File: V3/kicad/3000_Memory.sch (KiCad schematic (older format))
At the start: 4 parts, among them U3000 SST39SF040, U3001 AS6C4008-55PCN

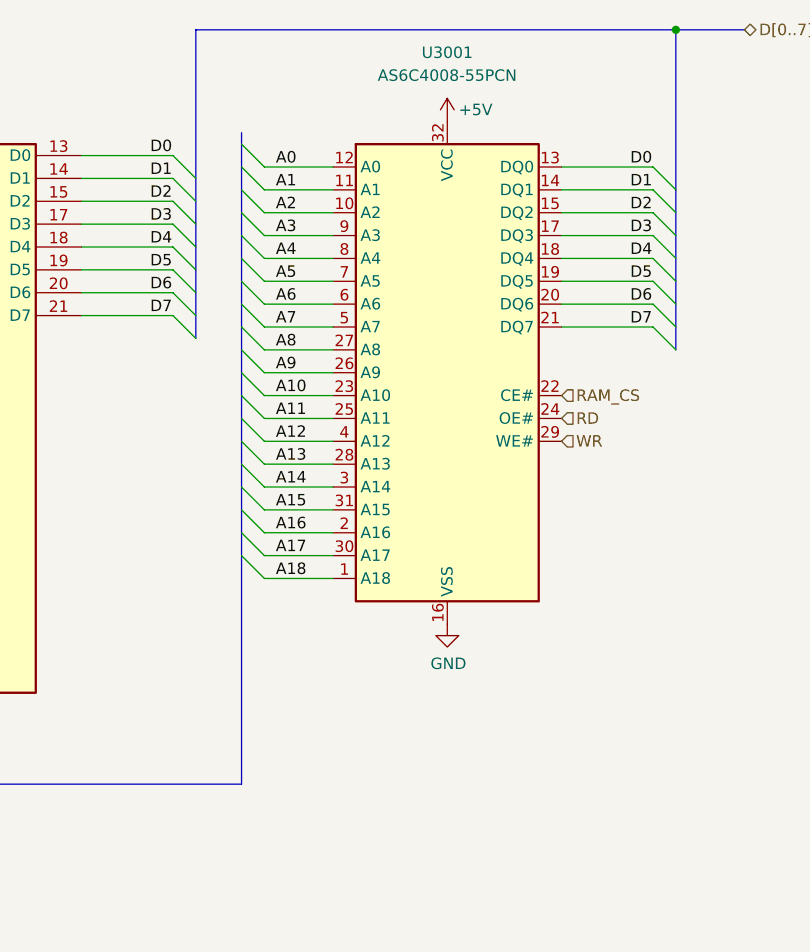
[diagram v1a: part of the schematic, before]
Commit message: Added new symbol and footprint
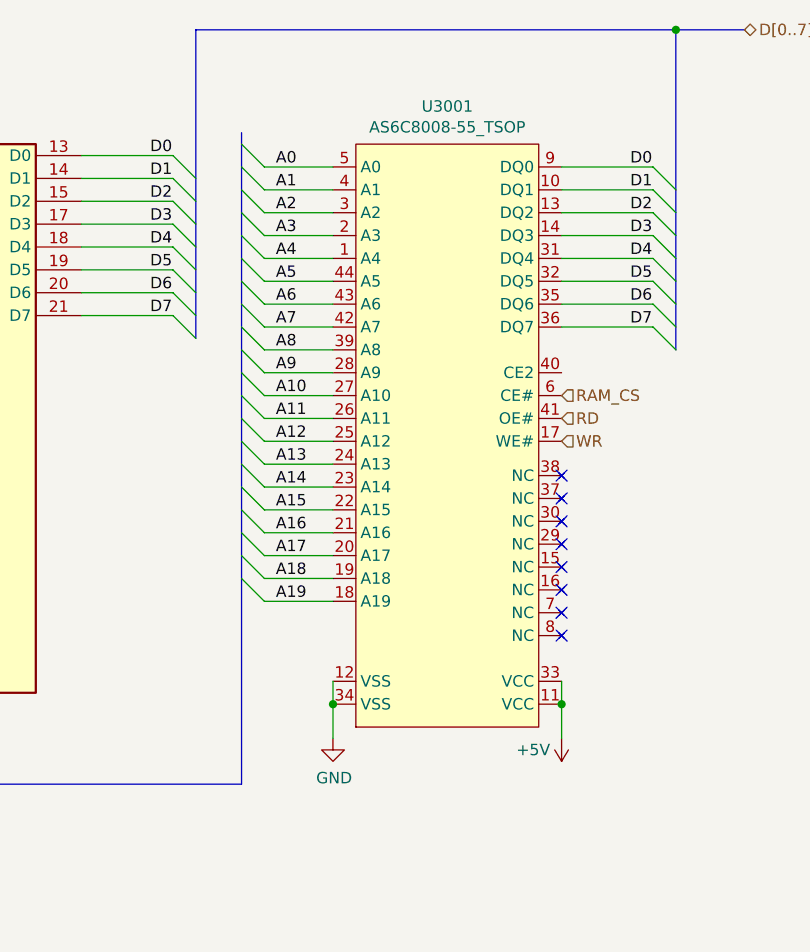
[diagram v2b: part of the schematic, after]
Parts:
- removed U3001: AS6C4008-55PCN, Package_SO:SSOP-32_11.305x20.495mm_P1.27mm, symbol Memory_RAM:AS6C4008-55PCN
- added U3001: AS6C8008-55_TSOP, Package_SO:TSOP-II-44_10.16x18.41mm_P0.8mm, symbol as6c8008-55_tsop:AS6C8008-55_TSOP
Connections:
- net +5V: now also U3001.11 (VCC), U3001.33 (VCC)
- net A0: now also U3001.5 (A0)
- net A1: now also U3001.4 (A1)
- net A10: now also U3001.27 (A10)
- net A11: now also U3001.26 (A11)
- net A12: now also U3001.25 (A12)
- net A13: now also U3001.24 (A13)
- net A14: now also U3001.23 (A14)
- net A15: now also U3001.22 (A15)
- net A16: now also U3001.21 (A16)
- net A17: now also U3001.20 (A17)
- net A18: now also U3001.19 (A18)
- net A2: now also U3001.3 (A2)
- net A3: now also U3001.2 (A3)
- net A4: now also U3001.1 (A4)
- net A5: now also U3001.44 (A5)
- net A6: now also U3001.43 (A6)
- net A7: now also U3001.42 (A7)
- net A8: now also U3001.39 (A8)
- net A9: now also U3001.28 (A9)
- net D0: now also U3001.9 (DQ0)
- net D1: now also U3001.10 (DQ1)
- net D2: now also U3001.13 (DQ2)
- net D3: now also U3001.14 (DQ3)
- net D4: now also U3001.31 (DQ4)
- net D5: now also U3001.32 (DQ5)
- net D6: now also U3001.35 (DQ6)
- net D7: now also U3001.36 (DQ7)
- net GND: now also U3001.12 (VSS), U3001.34 (VSS)
- net RAM_CS: now also U3001.6 (CE#)
- net RD: now also U3001.41 (OE#)
- net WR: now also U3001.17 (WE#)
- new net A19: U3001.18 (A19)
- no-connect marks 0 -> 8
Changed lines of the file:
@@
 Text Label 5300 3650 0    50   ~ 0
 D7
-Wire Bus Line
-	5500 2400 7600 2400
-Wire Bus Line
-	7600 2400 7900 2400
 Text HLabel 2800 5700 0    50   Input ~ 0
 A[0..19]
@@
 L power:+5V #PWR0180
 U 1 1 61F46407
-P 6600 2800
-F 0 "#PWR0180" H 6600 2650 50  0001 C CNN
-F 1 "+5V" H 6650 2850 50  0000 L CNN
-F 2 "" H 6600 2800 50  0001 C CNN
-F 3 "" H 6600 2800 50  0001 C CNN
-	1    6600 2800
-	1    0    0    -1
+P 7100 5500
+F 0 "#PWR0180" H 7100 5350 50  0001 C CNN
+F 1 "+5V" H 7150 5550 50  0000 L CNN
+F 2 "" H 7100 5500 50  0001 C CNN
+F 3 "" H 7100 5500 50  0001 C CNN
+	1    7100 5500
+	-1   0    0    1
 $EndComp
 $Comp
 L power:GND #PWR0181
 U 1 1 61F61A4C
-P 6600 5000
-F 0 "#PWR0181" H 6600 4750 50  0001 C CNN
-F 1 "GND" H 6605 4827 50  0000 C CNN
-F 2 "" H 6600 5000 50  0001 C CNN
-F 3 "" H 6600 5000 50  0001 C CNN
-	1    6600 5000
+P 6100 5500
+F 0 "#PWR0181" H 6100 5250 50  0001 C CNN
+F 1 "GND" H 6105 5327 50  0000 C CNN
+F 2 "" H 6100 5500 50  0001 C CNN
+F 3 "" H 6100 5500 50  0001 C CNN
+	1    6100 5500
 	1    0    0    -1
 $EndComp
@@
 	1    0    0    -1
 $EndComp
-$Comp
-L Memory_RAM:AS6C4008-55PCN U3001
-U 1 1 62109604
-P 6600 3900
-F 0 "U3001" H 6600 5300 50  0000 C CNN
-F 1 "AS6C4008-55PCN" H 6600 5200 50  0000 C CNN
-F 2 "Package_SO:SSOP-32_11.305x20.495mm_P1.27mm" H 6600 4000 50  0001 C CNN
-F 3 "https://www.digikey.com/en/products/detail/alliance-memory-inc/AS6C4008-55ZIN/4234590" H 6600 4000 50  0001 C CNN
-	1    6600 3900
-	1    0    0    -1
-$EndComp
 Text HLabel 7100 4000 2    50   Input ~ 0
 RAM_CS
 Text HLabel 3800 5150 0    50   Input ~ 0
 ROM_CS
-Connection ~ 7600 2400
 Entry Wire Line
 	3200 2850 3300 2950
@@
 	1    0    0    -1
 $EndComp
+$Comp
+L as6c8008-55_tsop:AS6C8008-55_TSOP U3001
+U 1 1 63A1386B
+P 6600 3900
+F 0 "U3001" H 6600 5065 50  0000 C CNN
+F 1 "AS6C8008-55_TSOP" H 6600 4974 50  0000 C CNN
+F 2 "Package_SO:TSOP-II-44_10.16x18.41mm_P0.8mm" H 6600 4973 50  0001 C CNN
+F 3 "https://www.alliancememory.com/wp-content/uploads/pdf/AS6C4008.pdf" H 6600 4000 50  0001 C CNN
+	1    6600 3900
+	1    0    0    -1
+$EndComp
+Entry Wire Line
+	5700 4800 5800 4900
+Wire Wire Line
+	5800 4900 6100 4900
+Text Label 5850 4900 0    50   ~ 0
+A19
+Wire Bus Line
+	5500 2400 7600 2400
+Connection ~ 7600 2400
+Wire Bus Line
+	7600 2400 7900 2400
+Wire Wire Line
+	7100 5250 7100 5350
+Connection ~ 7100 5350
+Wire Wire Line
+	7100 5350 7100 5500
+Wire Wire Line
+	6100 5250 6100 5350
+Connection ~ 6100 5350
+Wire Wire Line
+	6100 5350 6100 5500
+NoConn ~ 7100 4350
+NoConn ~ 7100 4450
+NoConn ~ 7100 4550
+NoConn ~ 7100 4650
+NoConn ~ 7100 4750
+NoConn ~ 7100 4850
+NoConn ~ 7100 4950
+NoConn ~ 7100 5050
 Wire Bus Line
 	5500 2400 5500 3750

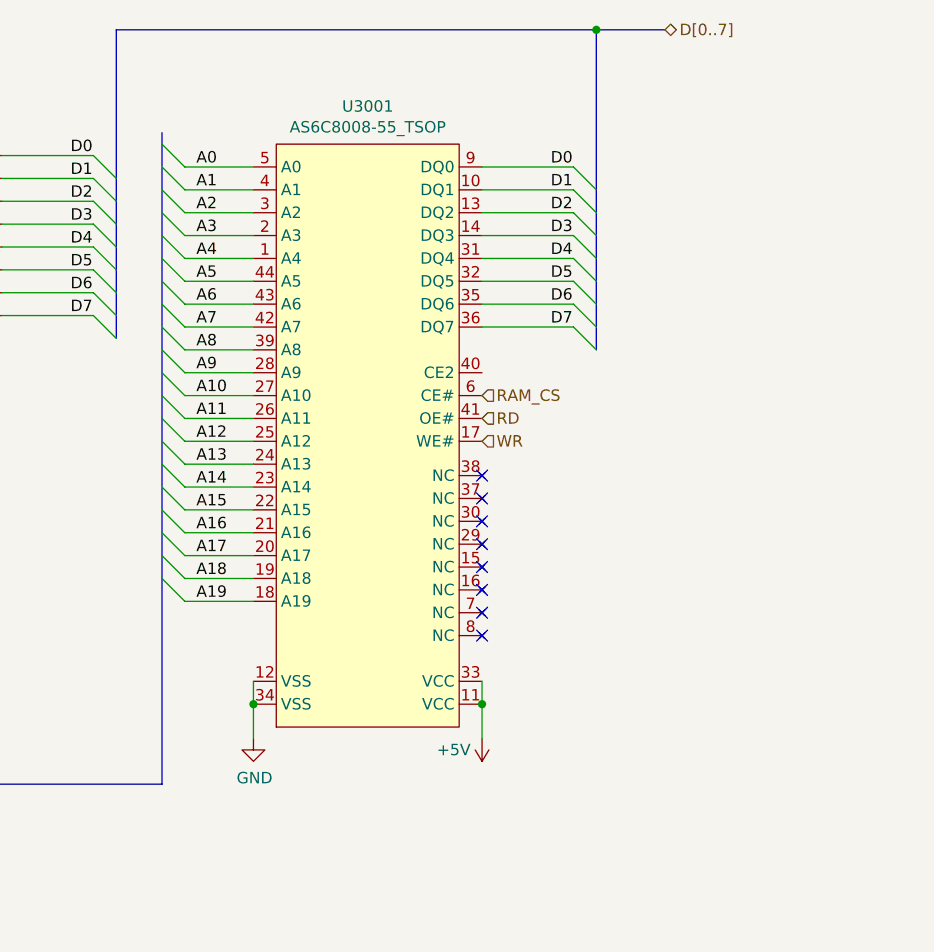
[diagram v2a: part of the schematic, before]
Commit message: Replace chip with PLCC, strip out uncritical elements
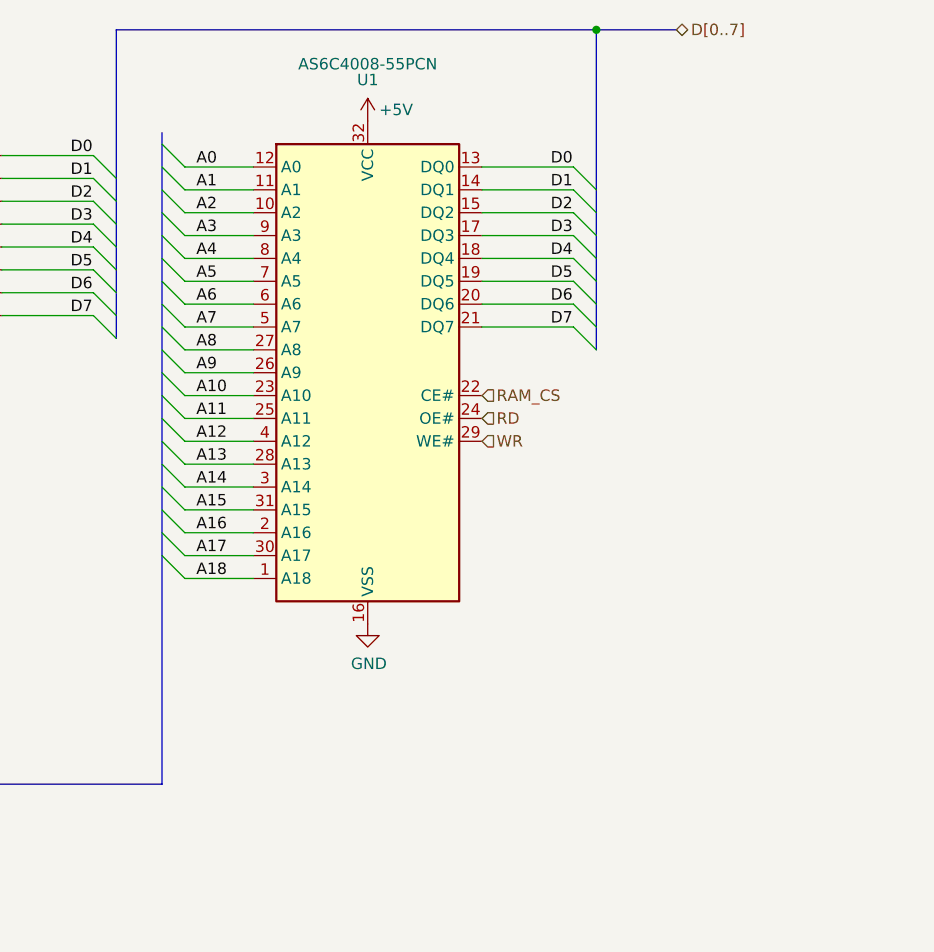
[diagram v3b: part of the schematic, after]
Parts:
- removed U3001: AS6C8008-55_TSOP, Package_SO:TSOP-II-44_10.16x18.41mm_P0.8mm, symbol as6c8008-55_tsop:AS6C8008-55_TSOP
- added U1: AS6C4008-55PCN, Package_DIP:DIP-32_W15.24mm_LongPads, symbol Memory_RAM:AS6C4008-55PCN
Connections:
- net +5V: now also U1.32 (VCC)
- net A0: now also U1.12 (A0)
- net A1: now also U1.11 (A1)
- net A10: now also U1.23 (A10)
- net A11: now also U1.25 (A11)
- net A12: now also U1.4 (A12)
- net A13: now also U1.28 (A13)
- net A14: now also U1.3 (A14)
- net A15: now also U1.31 (A15)
- net A16: now also U1.2 (A16)
- net A17: now also U1.30 (A17)
- net A18: now also U1.1 (A18)
- net A2: now also U1.10 (A2)
- net A3: now also U1.9 (A3)
- net A4: now also U1.8 (A4)
- net A5: now also U1.7 (A5)
- net A6: now also U1.6 (A6)
- net A7: now also U1.5 (A7)
- net A8: now also U1.27 (A8)
- net A9: now also U1.26 (A9)
- net D0: now also U1.13 (DQ0)
- net D1: now also U1.14 (DQ1)
- net D2: now also U1.15 (DQ2)
- net D3: now also U1.17 (DQ3)
- net D4: now also U1.18 (DQ4)
- net D5: now also U1.19 (DQ5)
- net D6: now also U1.20 (DQ6)
- net D7: now also U1.21 (DQ7)
- net GND: now also U1.16 (VSS)
- net RAM_CS: now also U1.22 (CE#)
- net RD: now also U1.24 (OE#)
- net WR: now also U1.29 (WE#)
- no-connect marks 8 -> 0
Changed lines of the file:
@@
 $Descr A4 11693 8268
 encoding utf-8
-Sheet 2 6
+Sheet 2 5
 Title ""
 Date ""
@@
 Text HLabel 2800 5700 0    50   Input ~ 0
 A[0..19]
-Text HLabel 7900 2400 2    50   BiDi ~ 0
+Text HLabel 7950 2400 2    50   BiDi ~ 0
 D[0..7]
 $Comp
@@
 L power:+5V #PWR0180
 U 1 1 61F46407
-P 7100 5500
-F 0 "#PWR0180" H 7100 5350 50  0001 C CNN
-F 1 "+5V" H 7150 5550 50  0000 L CNN
-F 2 "" H 7100 5500 50  0001 C CNN
-F 3 "" H 7100 5500 50  0001 C CNN
-	1    7100 5500
-	-1   0    0    1
+P 6600 2800
+F 0 "#PWR0180" H 6600 2650 50  0001 C CNN
+F 1 "+5V" H 6650 2850 50  0000 L CNN
+F 2 "" H 6600 2800 50  0001 C CNN
+F 3 "" H 6600 2800 50  0001 C CNN
+	1    6600 2800
+	1    0    0    -1
 $EndComp
 $Comp
 L power:GND #PWR0181
 U 1 1 61F61A4C
-P 6100 5500
-F 0 "#PWR0181" H 6100 5250 50  0001 C CNN
-F 1 "GND" H 6105 5327 50  0000 C CNN
-F 2 "" H 6100 5500 50  0001 C CNN
-F 3 "" H 6100 5500 50  0001 C CNN
-	1    6100 5500
+P 6600 5000
+F 0 "#PWR0181" H 6600 4750 50  0001 C CNN
+F 1 "GND" H 6605 4827 50  0000 C CNN
+F 2 "" H 6600 5000 50  0001 C CNN
+F 3 "" H 6600 5000 50  0001 C CNN
+	1    6600 5000
 	1    0    0    -1
 $EndComp
@@
 	1    0    0    -1
 $EndComp
-$Comp
-L as6c8008-55_tsop:AS6C8008-55_TSOP U3001
-U 1 1 63A1386B
+Wire Bus Line
+	5500 2400 7600 2400
+$Comp
+L Memory_RAM:AS6C4008-55PCN U1
+U 1 1 6545BB5D
 P 6600 3900
-F 0 "U3001" H 6600 5065 50  0000 C CNN
-F 1 "AS6C8008-55_TSOP" H 6600 4974 50  0000 C CNN
-F 2 "Package_SO:TSOP-II-44_10.16x18.41mm_P0.8mm" H 6600 4973 50  0001 C CNN
+F 0 "U1" H 6600 5181 50  0000 C CNN
+F 1 "AS6C4008-55PCN" H 6600 5250 50  0000 C CNN
+F 2 "Package_DIP:DIP-32_W15.24mm_LongPads" H 6600 4000 50  0001 C CNN
 F 3 "https://www.alliancememory.com/wp-content/uploads/pdf/AS6C4008.pdf" H 6600 4000 50  0001 C CNN
 	1    6600 3900
 	1    0    0    -1
 $EndComp
-Entry Wire Line
-	5700 4800 5800 4900
-Wire Wire Line
-	5800 4900 6100 4900
-Text Label 5850 4900 0    50   ~ 0
-A19
-Wire Bus Line
-	5500 2400 7600 2400
+Wire Bus Line
+	7600 2400 7950 2400
+Wire Bus Line
+	5500 2400 5500 3750
+Wire Bus Line
+	7600 2400 7600 3800
+Wire Bus Line
+	5700 2850 5700 5700
+Wire Bus Line
+	3200 2850 3200 5700
 Connection ~ 7600 2400
-Wire Bus Line
-	7600 2400 7900 2400
-Wire Wire Line
-	7100 5250 7100 5350
-Connection ~ 7100 5350
-Wire Wire Line
-	7100 5350 7100 5500
-Wire Wire Line
-	6100 5250 6100 5350
-Connection ~ 6100 5350
-Wire Wire Line
-	6100 5350 6100 5500
-NoConn ~ 7100 4350
-NoConn ~ 7100 4450
-NoConn ~ 7100 4550
-NoConn ~ 7100 4650
-NoConn ~ 7100 4750
-NoConn ~ 7100 4850
-NoConn ~ 7100 4950
-NoConn ~ 7100 5050
-Wire Bus Line
-	5500 2400 5500 3750
-Wire Bus Line
-	7600 2400 7600 3800
-Wire Bus Line
-	5700 2850 5700 5700
-Wire Bus Line
-	3200 2850 3200 5700
 $EndSCHEMATC
